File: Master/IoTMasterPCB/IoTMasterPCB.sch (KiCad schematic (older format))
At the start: 0 parts

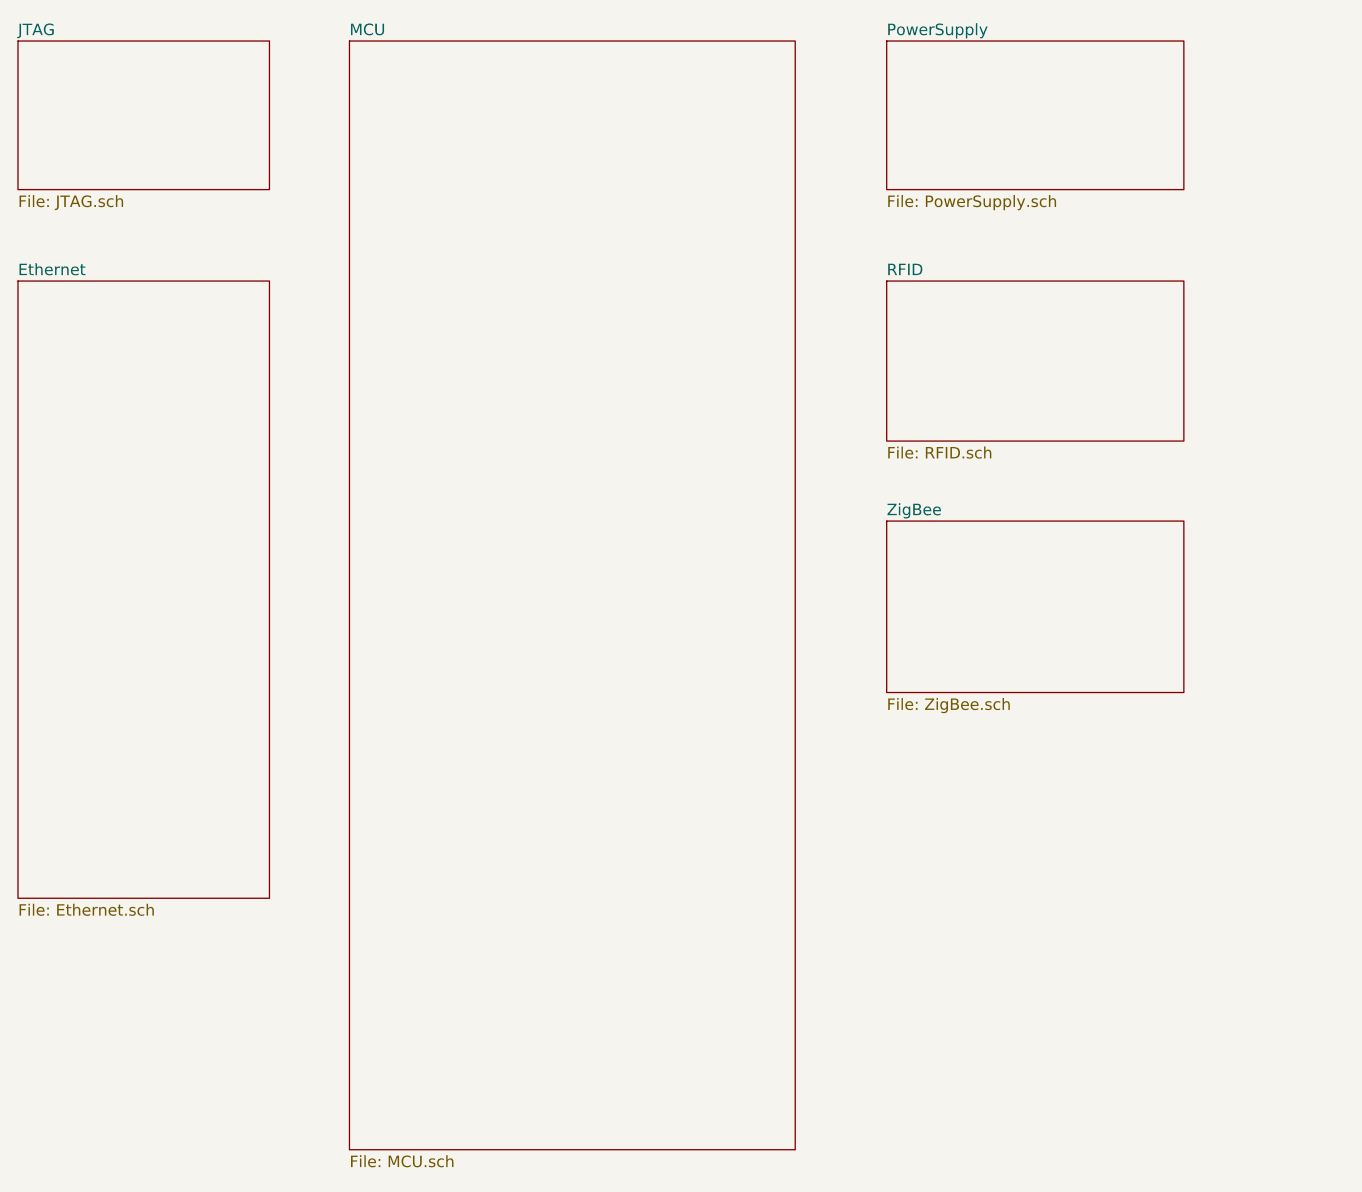
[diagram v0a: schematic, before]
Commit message: Updated Master Board schematics. Added JTAG connector.
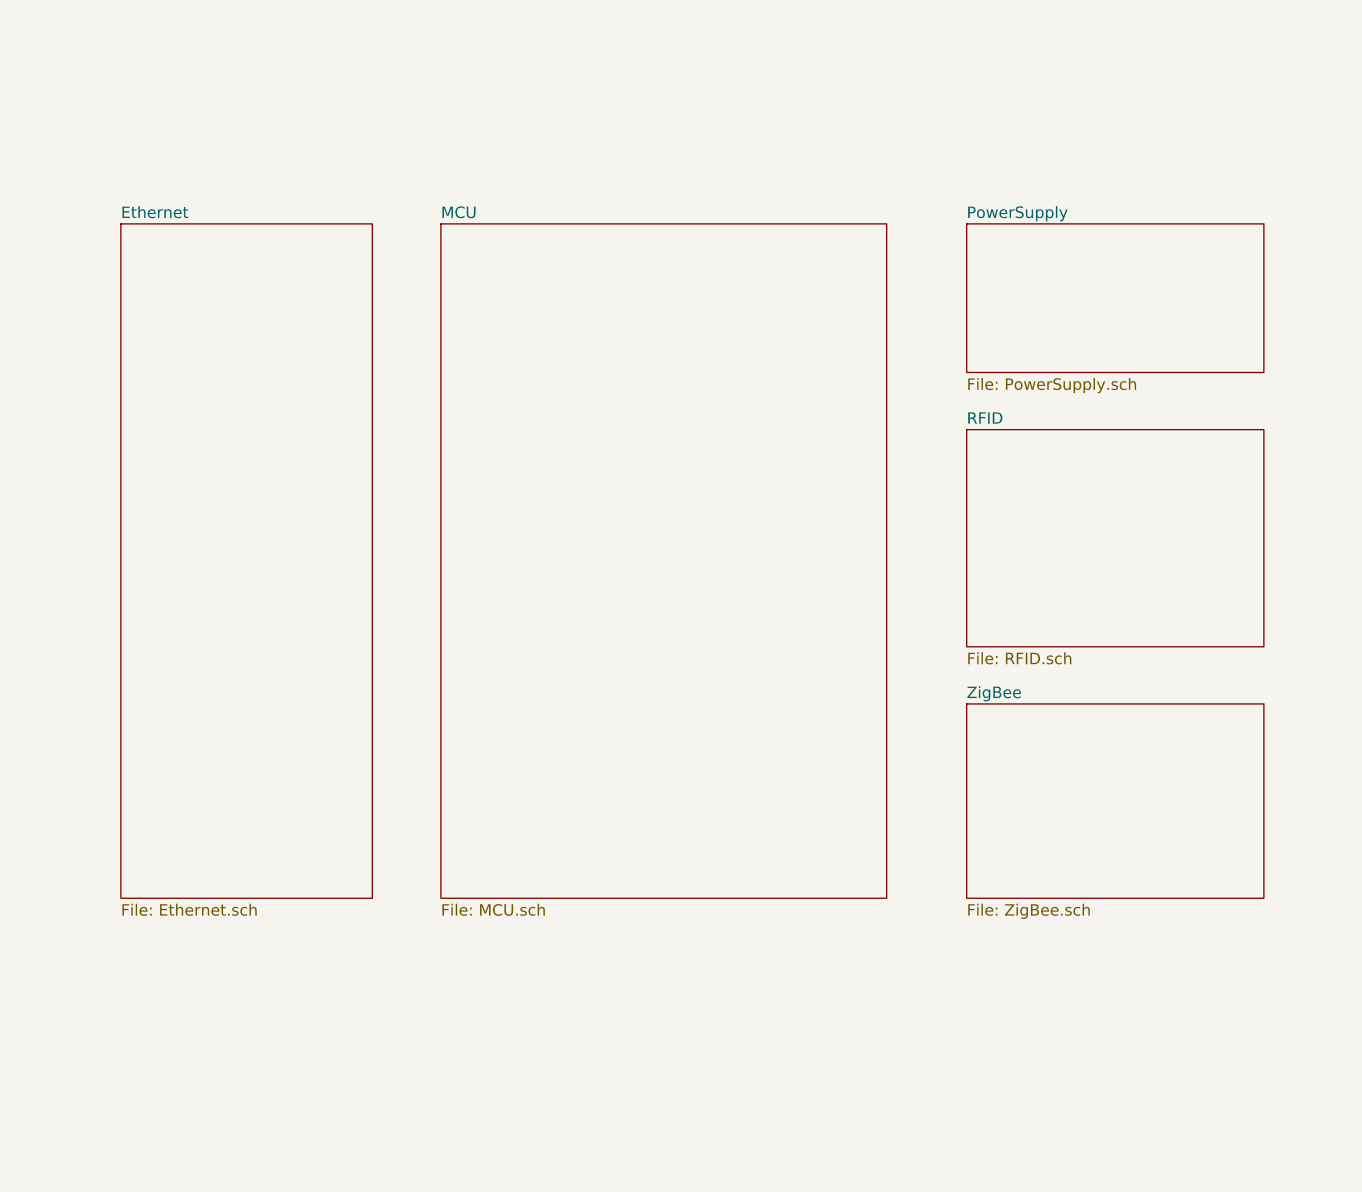
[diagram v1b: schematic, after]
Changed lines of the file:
@@
 $Descr A4 11693 8268
 encoding utf-8
-Sheet 1 7
+Sheet 1 6
 Title "IoT Master Board"
-Date "2020-11-01"
+Date "2020-11-28"
 Rev "1.0"
 Comp "University of Southern Denmark"
@@
 $EndDescr
 $Sheet
-S 4200 1400 1950 4850
+S 4600 2200 1950 2950
 U 5F9E799A
 F0 "MCU" 50
@@
 $EndSheet
 $Sheet
-S 2750 1400 1100 650
-U 5F9EEBEE
-F0 "JTAG" 50
-F1 "JTAG.sch" 50
-$EndSheet
-$Sheet
-S 6550 1400 1300 650
+S 6900 2200 1300 650
 U 5F9EEC7C
 F0 "PowerSupply" 50
@@
 $EndSheet
 $Sheet
-S 6550 2450 1300 700
+S 6900 3100 1300 950
 U 5F9EEDC0
 F0 "RFID" 50
@@
 $EndSheet
 $Sheet
-S 6550 3500 1300 750
+S 6900 4300 1300 850
 U 5F9EEE30
 F0 "ZigBee" 50
@@
 $EndSheet
 $Sheet
-S 2750 2450 1100 2700
+S 3200 2200 1100 2950
 U 5F9EEF53
 F0 "Ethernet" 50

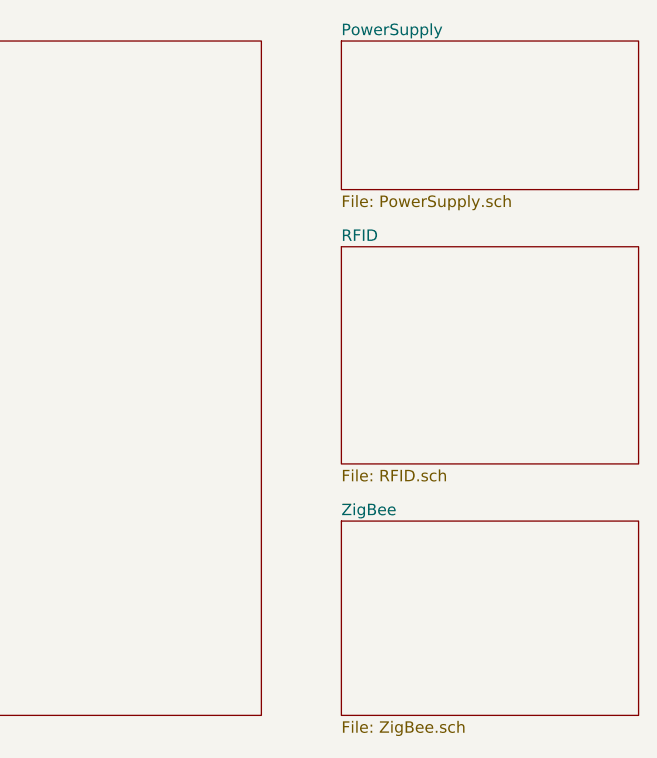
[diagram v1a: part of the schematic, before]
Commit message: Work on Master Board schematics; added full Zigbee. Added RFID module. Added USB/power supply, as well as MCU decoupling.
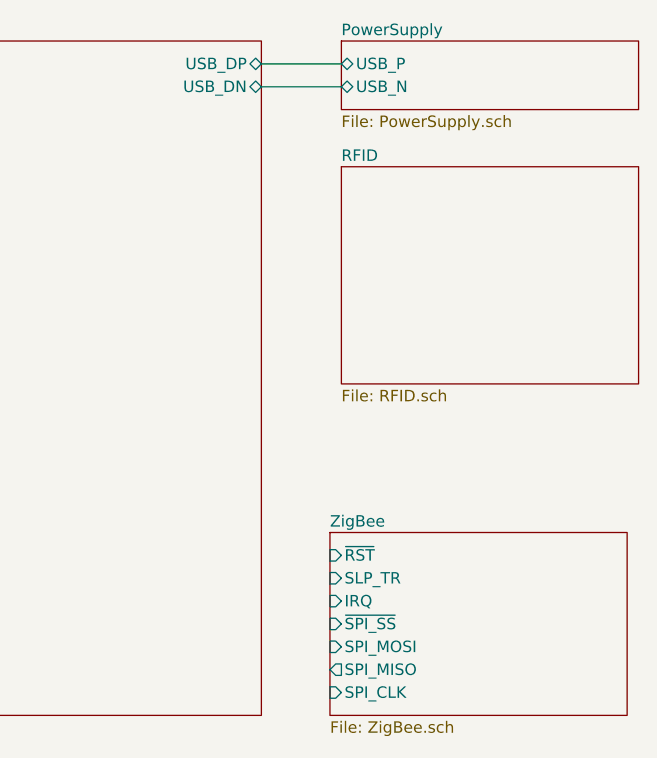
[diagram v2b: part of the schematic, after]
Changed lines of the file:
@@
 F0 "MCU" 50
 F1 "MCU.sch" 50
+F2 "USB_DP" B R 6550 2300 50
+F3 "USB_DN" B R 6550 2400 50
 $EndSheet
 $Sheet
-S 6900 2200 1300 650
+S 6900 2200 1300 300
 U 5F9EEC7C
 F0 "PowerSupply" 50
 F1 "PowerSupply.sch" 50
+F2 "USB_P" B L 6900 2300 50
+F3 "USB_N" B L 6900 2400 50
 $EndSheet
 $Sheet
-S 6900 3100 1300 950
+S 6900 2750 1300 950
 U 5F9EEDC0
 F0 "RFID" 50
@@
 $EndSheet
 $Sheet
-S 6900 4300 1300 850
+S 6850 4350 1300 800
 U 5F9EEE30
 F0 "ZigBee" 50
 F1 "ZigBee.sch" 50
+F2 "~RST" I L 6850 4450 50
+F3 "SLP_TR" I L 6850 4550 50
+F4 "IRQ" I L 6850 4650 50
+F5 "~SPI_SS" I L 6850 4750 50
+F6 "SPI_MOSI" I L 6850 4850 50
+F7 "SPI_CLK" I L 6850 5050 50
+F8 "SPI_MISO" O L 6850 4950 50
 $EndSheet
 $Sheet
@@
 F1 "Ethernet.sch" 50
 $EndSheet
+Wire Wire Line
+	6550 2300 6900 2300
+Wire Wire Line
+	6900 2400 6550 2400
 $EndSCHEMATC

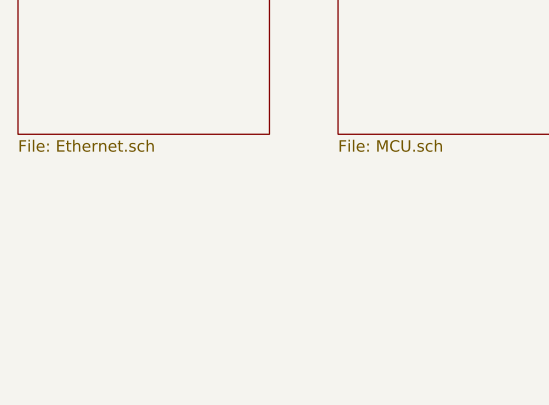
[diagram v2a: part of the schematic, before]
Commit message: Added flash storage, work on RFID front-end.
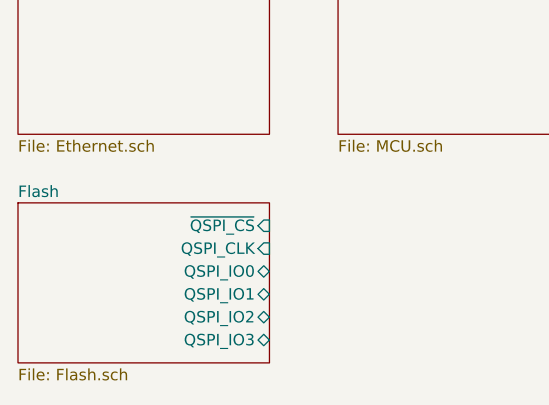
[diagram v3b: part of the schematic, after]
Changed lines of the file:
@@
 $Descr A4 11693 8268
 encoding utf-8
-Sheet 1 6
+Sheet 1 7
 Title "IoT Master Board"
 Date "2020-11-28"
@@
 Wire Wire Line
 	6900 2400 6550 2400
+$Sheet
+S 3200 5450 1100 700
+U 5FCEA9CB
+F0 "Flash" 50
+F1 "Flash.sch" 50
+F2 "~QSPI_CS" I R 4300 5550 50
+F3 "QSPI_CLK" I R 4300 5650 50
+F4 "QSPI_IO0" B R 4300 5750 50
+F5 "QSPI_IO1" B R 4300 5850 50
+F6 "QSPI_IO2" B R 4300 5950 50
+F7 "QSPI_IO3" B R 4300 6050 50
+$EndSheet
 $EndSCHEMATC

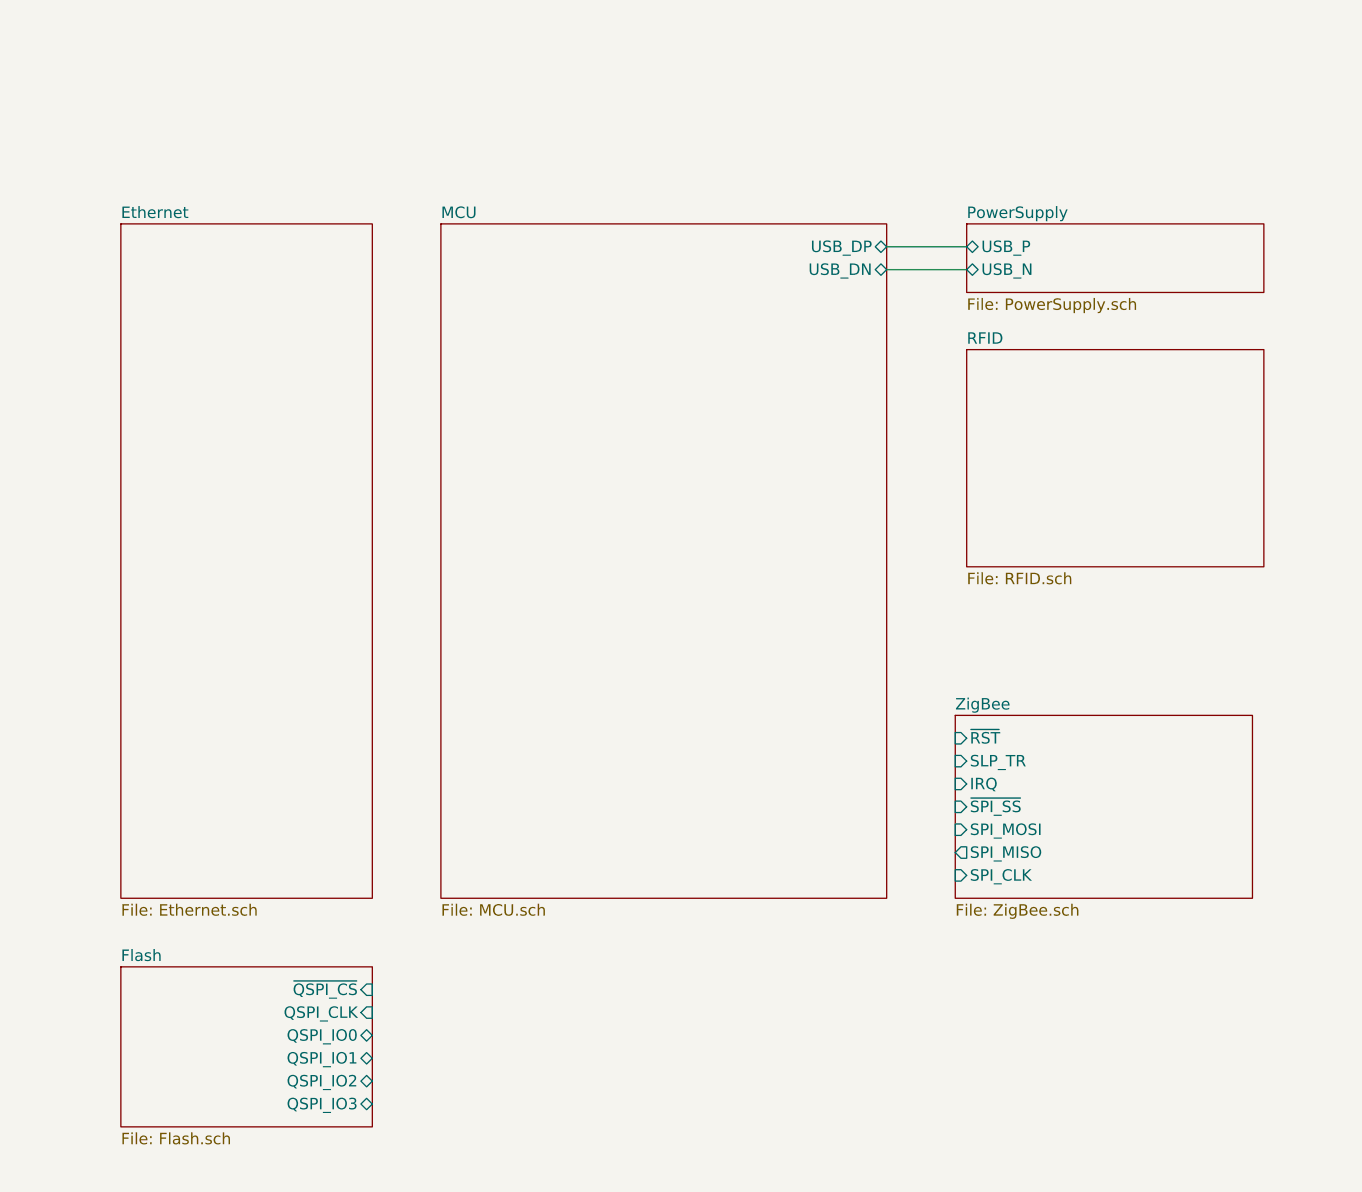
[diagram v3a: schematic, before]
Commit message: Finished RFID module sans antenna footprint. Added KSZ8081MNX and hierarchial connections.
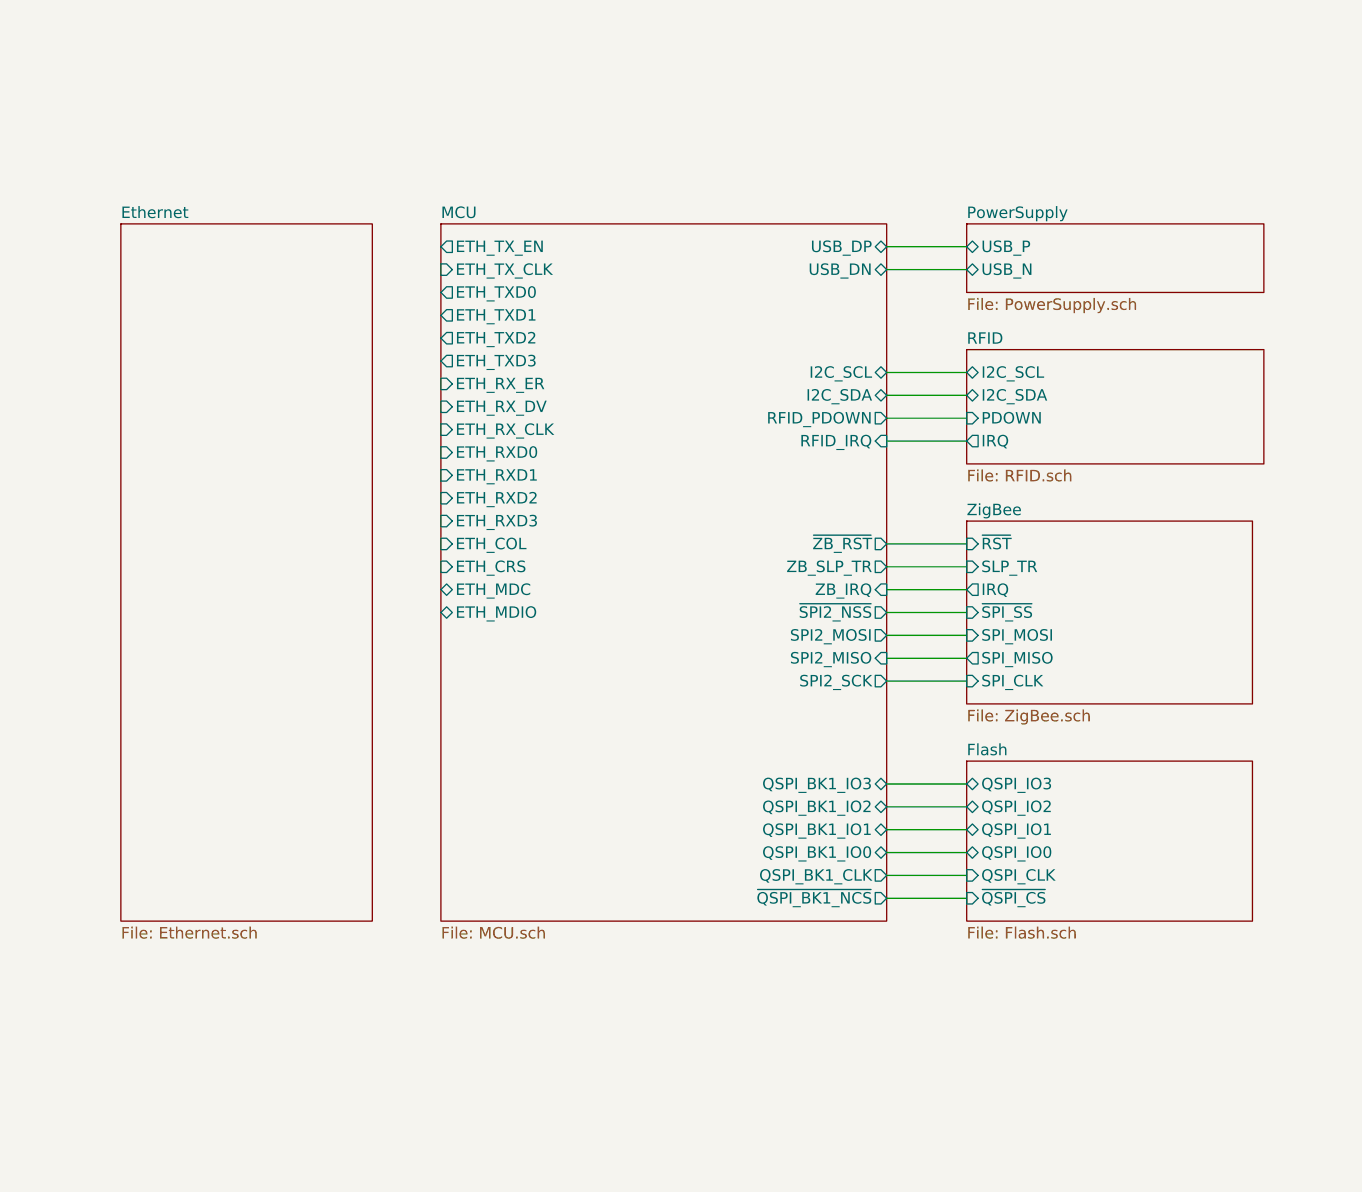
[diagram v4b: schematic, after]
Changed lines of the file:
@@
 $EndDescr
 $Sheet
-S 4600 2200 1950 2950
+S 4600 2200 1950 3050
 U 5F9E799A
 F0 "MCU" 50
@@
 F2 "USB_DP" B R 6550 2300 50
 F3 "USB_DN" B R 6550 2400 50
+F4 "SPI2_SCK" O R 6550 4200 50
+F5 "SPI2_MOSI" O R 6550 4000 50
+F6 "~SPI2_NSS" O R 6550 3900 50
+F7 "ZB_SLP_TR" O R 6550 3700 50
+F8 "~ZB_RST" O R 6550 3600 50
+F9 "SPI2_MISO" I R 6550 4100 50
+F10 "ZB_IRQ" I R 6550 3800 50
+F11 "~QSPI_BK1_NCS" O R 6550 5150 50
+F12 "QSPI_BK1_CLK" O R 6550 5050 50
+F13 "QSPI_BK1_IO0" B R 6550 4950 50
+F14 "QSPI_BK1_IO1" B R 6550 4850 50
+F15 "QSPI_BK1_IO2" B R 6550 4750 50
+F16 "QSPI_BK1_IO3" B R 6550 4650 50
+F17 "I2C_SCL" B R 6550 2850 50
+F18 "I2C_SDA" B R 6550 2950 50
+F19 "RFID_PDOWN" O R 6550 3050 50
+F20 "RFID_IRQ" I R 6550 3150 50
+F21 "ETH_TX_EN" O L 4600 2300 50
+F22 "ETH_TX_CLK" I L 4600 2400 50
+F23 "ETH_TXD0" O L 4600 2500 50
+F24 "ETH_TXD1" O L 4600 2600 50
+F25 "ETH_TXD2" O L 4600 2700 50
+F26 "ETH_TXD3" O L 4600 2800 50
+F27 "ETH_RX_ER" I L 4600 2900 50
+F28 "ETH_RX_DV" I L 4600 3000 50
+F29 "ETH_RX_CLK" I L 4600 3100 50
+F30 "ETH_RXD0" I L 4600 3200 50
+F31 "ETH_RXD1" I L 4600 3300 50
+F32 "ETH_RXD2" I L 4600 3400 50
+F33 "ETH_RXD3" I L 4600 3500 50
+F34 "ETH_COL" I L 4600 3600 50
+F35 "ETH_CRS" I L 4600 3700 50
+F36 "ETH_MDC" B L 4600 3800 50
+F37 "ETH_MDIO" B L 4600 3900 50
 $EndSheet
 $Sheet
@@
 $EndSheet
 $Sheet
-S 6900 2750 1300 950
+S 6900 2750 1300 500
 U 5F9EEDC0
 F0 "RFID" 50
 F1 "RFID.sch" 50
+F2 "PDOWN" I L 6900 3050 50
+F3 "I2C_SCL" B L 6900 2850 50
+F4 "I2C_SDA" B L 6900 2950 50
+F5 "IRQ" O L 6900 3150 50
 $EndSheet
 $Sheet
-S 6850 4350 1300 800
+S 6900 3500 1250 800
 U 5F9EEE30
 F0 "ZigBee" 50
 F1 "ZigBee.sch" 50
-F2 "~RST" I L 6850 4450 50
-F3 "SLP_TR" I L 6850 4550 50
-F4 "IRQ" I L 6850 4650 50
-F5 "~SPI_SS" I L 6850 4750 50
-F6 "SPI_MOSI" I L 6850 4850 50
-F7 "SPI_CLK" I L 6850 5050 50
-F8 "SPI_MISO" O L 6850 4950 50
+F2 "~RST" I L 6900 3600 50
+F3 "SLP_TR" I L 6900 3700 50
+F4 "IRQ" O L 6900 3800 50
+F5 "~SPI_SS" I L 6900 3900 50
+F6 "SPI_MOSI" I L 6900 4000 50
+F7 "SPI_CLK" I L 6900 4200 50
+F8 "SPI_MISO" O L 6900 4100 50
 $EndSheet
 $Sheet
-S 3200 2200 1100 2950
+S 3200 2200 1100 3050
 U 5F9EEF53
 F0 "Ethernet" 50
@@
 	6900 2400 6550 2400
 $Sheet
-S 3200 5450 1100 700
+S 6900 4550 1250 700
 U 5FCEA9CB
 F0 "Flash" 50
 F1 "Flash.sch" 50
-F2 "~QSPI_CS" I R 4300 5550 50
-F3 "QSPI_CLK" I R 4300 5650 50
-F4 "QSPI_IO0" B R 4300 5750 50
-F5 "QSPI_IO1" B R 4300 5850 50
-F6 "QSPI_IO2" B R 4300 5950 50
-F7 "QSPI_IO3" B R 4300 6050 50
+F2 "~QSPI_CS" I L 6900 5150 50
+F3 "QSPI_CLK" I L 6900 5050 50
+F4 "QSPI_IO0" B L 6900 4950 50
+F5 "QSPI_IO1" B L 6900 4850 50
+F6 "QSPI_IO2" B L 6900 4750 50
+F7 "QSPI_IO3" B L 6900 4650 50
 $EndSheet
+Wire Wire Line
+	6550 3600 6900 3600
+Wire Wire Line
+	6900 3700 6550 3700
+Wire Wire Line
+	6550 3800 6900 3800
+Wire Wire Line
+	6900 3900 6550 3900
+Wire Wire Line
+	6550 4000 6900 4000
+Wire Wire Line
+	6900 4100 6550 4100
+Wire Wire Line
+	6550 4200 6900 4200
+Wire Wire Line
+	6550 5150 6900 5150
+Wire Wire Line
+	6550 5050 6900 5050
+Wire Wire Line
+	6550 4950 6900 4950
+Wire Wire Line
+	6550 4850 6900 4850
+Wire Wire Line
+	6550 4750 6900 4750
+Wire Wire Line
+	6550 4650 6900 4650
+Wire Wire Line
+	6550 3150 6900 3150
+Wire Wire Line
+	6900 3050 6550 3050
+Wire Wire Line
+	6550 2950 6900 2950
+Wire Wire Line
+	6900 2850 6550 2850
 $EndSCHEMATC
